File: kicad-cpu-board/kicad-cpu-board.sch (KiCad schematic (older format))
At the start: 56 parts, among them J101 ICSP Header, J102 Conn_01x10_Male, J103 Conn_01x15_Female, J104 Conn_02x05_Odd_Even, Q101 2N7000, Q102 2N7000, Q103 2N7000, Q104 2N7000, U101 L7805, U102 LP2950-3.3_TO92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

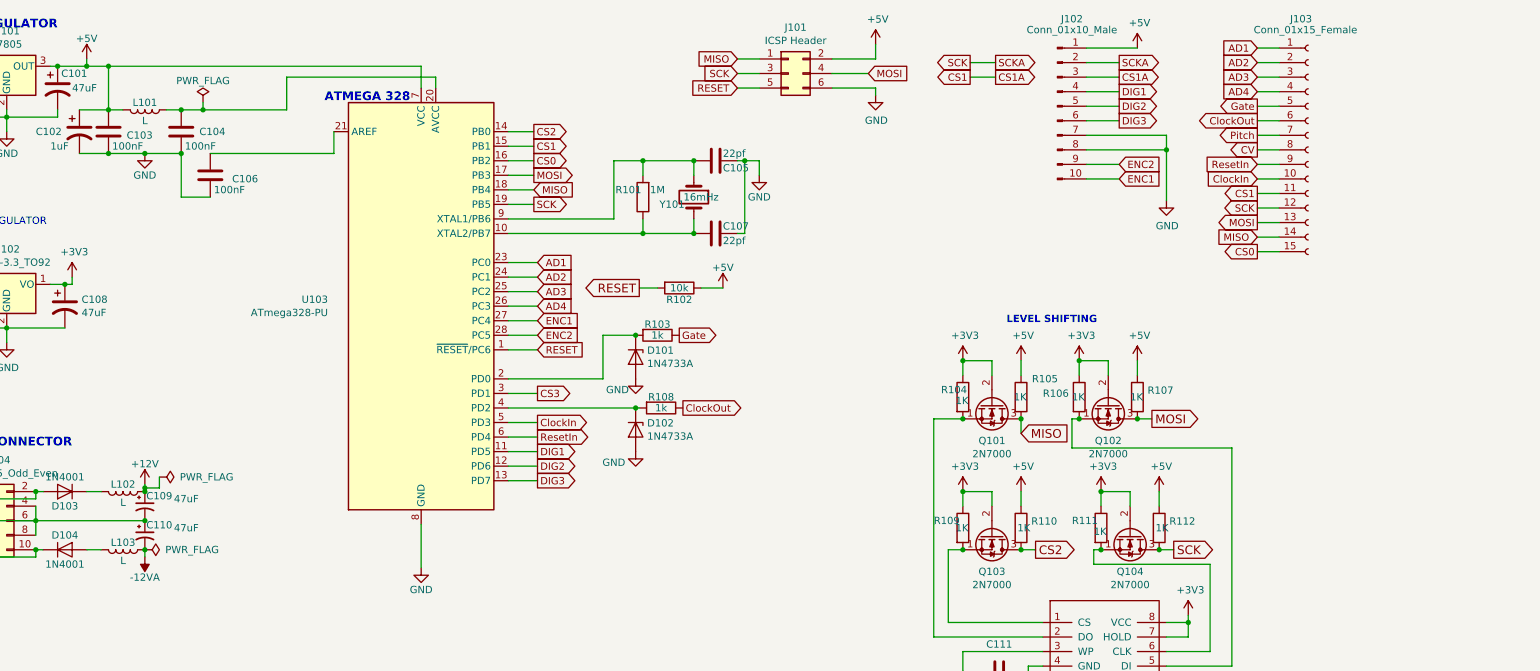
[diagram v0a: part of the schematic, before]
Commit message: Updating PCB and schematics for assembly bugfixes
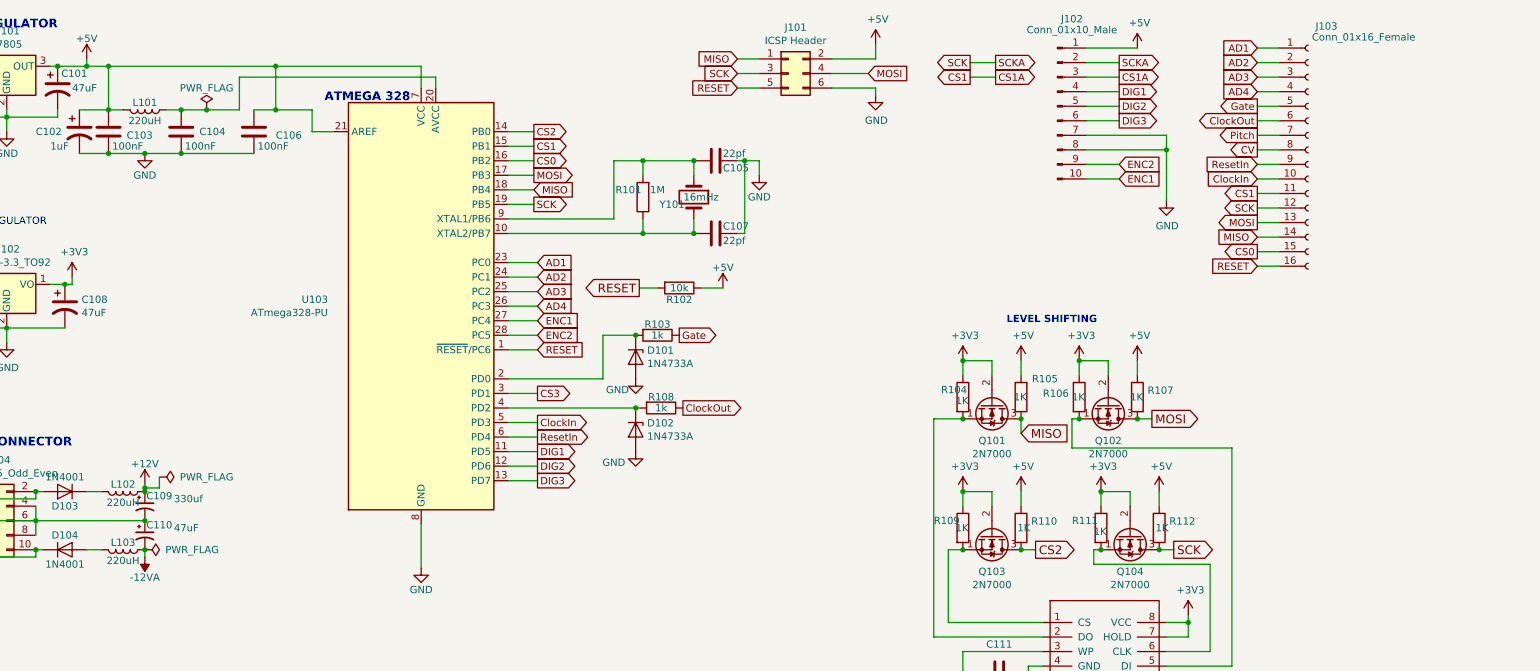
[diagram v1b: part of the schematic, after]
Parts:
- removed J103: Conn_01x15_Female, Pin_Headers:Pin_Header_Straight_1x15_Pitch2.54mm, symbol Connector:Conn_01x15_Female
- added J103: Conn_01x16_Female, Pin_Headers:Pin_Header_Straight_1x16_Pitch2.54mm, symbol Connector:Conn_01x16_Female
- C109: value 47uF -> 330uf
- L101, L102, L103: value L -> 220uH; footprint Inductors_THT:L_Axial_L5.3mm_D2.2mm_P7.62mm_Horizontal_Vishay_IM-1 -> Inductors_THT:L_Axial_L6.6mm_D2.7mm_P10.16mm_Horizontal_Vishay_IM-2
- Q101, Q102, Q103, Q104, U102: footprint TO_SOT_Packages_THT:TO-92_Inline_Narrow_Oval -> TO_SOT_Packages_THT:TO-92_Inline_Wide
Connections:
- net +5V: now also C106.1, U103.21 (AREF)
- net AD1: now also J103.1 (Pin_1)
- net AD2: now also J103.2 (Pin_2)
- net AD3: now also J103.3 (Pin_3)
- net AD4: now also J103.4 (Pin_4)
- net CS0: now also J103.15 (Pin_15)
- net CS1: now also J103.11 (Pin_11)
- net CV: now also J103.8 (Pin_8)
- net ClockIn: now also J103.10 (Pin_10)
- net ClockOut: now also J103.6 (Pin_6)
- net Gate: now also J103.5 (Pin_5)
- net MISO: now also J103.14 (Pin_14)
- net MOSI: now also J103.13 (Pin_13)
- net Pitch: now also J103.7 (Pin_7)
- net RESET: now also J103.16 (Pin_16)
- net ResetIn: now also J103.9 (Pin_9)
- net SCK: now also J103.12 (Pin_12)
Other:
- moved on the sheet: C106
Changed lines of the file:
@@
 P 2625 1400
 F 0 "L101" V 2575 1400 50  0000 C CNN
-F 1 "L" V 2700 1400 50  0000 C CNN
-F 2 "Inductors_THT:L_Axial_L5.3mm_D2.2mm_P7.62mm_Horizontal_Vishay_IM-1" H 2625 1400 50  0001 C CNN
+F 1 "220uH" V 2700 1400 50  0000 C CNN
+F 2 "Inductors_THT:L_Axial_L6.6mm_D2.7mm_P10.16mm_Horizontal_Vishay_IM-2" H 2625 1400 50  0001 C CNN
 F 3 "" H 2625 1400 50  0001 C CNN
 	1    2625 1400
@@
 L Device:C C106
 U 1 1 5CE4BC80
-P 3075 1850
-F 0 "C106" H 3225 1825 50  0000 L CNN
-F 1 "100nF" H 3100 1750 50  0000 L CNN
-F 2 "Capacitors_THT:C_Disc_D5.0mm_W2.5mm_P2.50mm" H 3113 1700 50  0001 C CNN
-F 3 "" H 3075 1850 50  0001 C CNN
-	1    3075 1850
+P 3375 1550
+F 0 "C106" H 3525 1525 50  0000 L CNN
+F 1 "100nF" H 3400 1450 50  0000 L CNN
+F 2 "Capacitors_THT:C_Disc_D5.0mm_W2.5mm_P2.50mm" H 3413 1400 50  0001 C CNN
+F 3 "" H 3375 1550 50  0001 C CNN
+	1    3375 1550
 	1    0    0    -1
 $EndComp
@@
 Wire Wire Line
 	2375 1700 2625 1700
-Wire Wire Line
-	2875 1700 2875 2000
-Wire Wire Line
-	2875 2000 3075 2000
 Connection ~ 2875 1400
 Wire Wire Line
@@
 L power:PWR_FLAG #FLG0101
 U 1 1 5B3B3D9E
-P 3025 1350
-F 0 "#FLG0101" H 3025 1425 50  0001 C CNN
-F 1 "PWR_FLAG" H 3025 1500 50  0000 C CNN
-F 2 "" H 3025 1350 50  0001 C CNN
-F 3 "" H 3025 1350 50  0001 C CNN
-	1    3025 1350
-	1    0    0    -1
-$EndComp
-Wire Wire Line
-	3025 1350 3025 1400
-Connection ~ 3025 1400
+P 3050 1400
+F 0 "#FLG0101" H 3050 1475 50  0001 C CNN
+F 1 "PWR_FLAG" H 3050 1550 50  0000 C CNN
+F 2 "" H 3050 1400 50  0001 C CNN
+F 3 "" H 3050 1400 50  0001 C CNN
+	1    3050 1400
+	1    0    0    -1
+$EndComp
 Wire Wire Line
 	2625 1700 2875 1700
-Wire Wire Line
-	2875 1400 3025 1400
 Wire Wire Line
 	2225 1100 2375 1100
@@
 F 0 "Q103" V 8700 4325 50  0000 C CNN
 F 1 "2N7000" V 8791 4325 50  0000 C CNN
-F 2 "TO_SOT_Packages_THT:TO-92_Inline_Narrow_Oval" H 8650 4250 50  0001 L CIN
+F 2 "TO_SOT_Packages_THT:TO-92_Inline_Wide" H 8650 4250 50  0001 L CIN
 F 3 "https://www.fairchildsemi.com/datasheets/2N/2N7000.pdf" H 8450 4325 50  0001 L CNN
 	1    8450 4325
@@
 F 0 "Q104" V 9650 4325 50  0000 C CNN
 F 1 "2N7000" V 9741 4325 50  0000 C CNN
-F 2 "TO_SOT_Packages_THT:TO-92_Inline_Narrow_Oval" H 9600 4250 50  0001 L CIN
+F 2 "TO_SOT_Packages_THT:TO-92_Inline_Wide" H 9600 4250 50  0001 L CIN
 F 3 "https://www.fairchildsemi.com/datasheets/2N/2N7000.pdf" H 9400 4325 50  0001 L CNN
 	1    9400 4325
@@
 F 0 "Q101" V 8700 3425 50  0000 C CNN
 F 1 "2N7000" V 8791 3425 50  0000 C CNN
-F 2 "TO_SOT_Packages_THT:TO-92_Inline_Narrow_Oval" H 8650 3350 50  0001 L CIN
+F 2 "TO_SOT_Packages_THT:TO-92_Inline_Wide" H 8650 3350 50  0001 L CIN
 F 3 "https://www.fairchildsemi.com/datasheets/2N/2N7000.pdf" H 8450 3425 50  0001 L CNN
 	1    8450 3425
@@
 F 0 "Q102" V 9500 3425 50  0000 C CNN
 F 1 "2N7000" V 9591 3425 50  0000 C CNN
-F 2 "TO_SOT_Packages_THT:TO-92_Inline_Narrow_Oval" H 9450 3350 50  0001 L CIN
+F 2 "TO_SOT_Packages_THT:TO-92_Inline_Wide" H 9450 3350 50  0001 L CIN
 F 3 "https://www.fairchildsemi.com/datasheets/2N/2N7000.pdf" H 9250 3425 50  0001 L CNN
 	1    9250 3425
@@
 F 0 "U102" H 1675 2842 50  0000 C CNN
 F 1 "LP2950-3.3_TO92" H 1675 2751 50  0000 C CNN
-F 2 "TO_SOT_Packages_THT:TO-92_Inline_Narrow_Oval" H 1675 2825 50  0001 C CIN
+F 2 "TO_SOT_Packages_THT:TO-92_Inline_Wide" H 1675 2825 50  0001 C CIN
 F 3 "http://www.ti.com/lit/ds/symlink/lp2950-n.pdf" H 1675 2550 50  0001 C CNN
 	1    1675 2600
@@
 	5125 2450 5325 2450
 $Comp
-L Connector:Conn_01x15_Female J103
-U 1 1 5DCFED35
-P 10625 1675
-F 0 "J103" H 10500 2575 50  0000 L CNN
-F 1 "Conn_01x15_Female" H 10250 2500 50  0000 L CNN
-F 2 "Pin_Headers:Pin_Header_Straight_1x15_Pitch2.54mm" H 10625 1675 50  0001 C CNN
-F 3 "~" H 10625 1675 50  0001 C CNN
-	1    10625 1675
-	1    0    0    -1
-$EndComp
-$Comp
 L Connector:Conn_01x10_Male J102
 U 1 1 5DCFEE3D
@@
 	4525 1100 4525 1250
 Wire Wire Line
-	2375 1100 4525 1100
-Wire Wire Line
-	3600 1400 3600 1175
-Wire Wire Line
-	3600 1175 4625 1175
-Wire Wire Line
 	4625 1175 4625 1250
-Wire Wire Line
-	3025 1400 3600 1400
 $Comp
 L Regulator_Linear:L7805 U101
@@
 	1    0    0    -1
 $EndComp
-Connection ~ 2875 1700
 $Comp
 L power:+12V #PWR0133
@@
 	0    1    1    0
 $EndComp
-Wire Wire Line
-	3925 1700 3925 1550
-Wire Wire Line
-	3075 1700 3925 1700
 Wire Wire Line
 	4525 4250 4525 4550
@@
 $EndComp
 $Comp
-L Device:L L103
-U 1 1 5CE903D5
-P 2475 4425
-F 0 "L103" V 2425 4425 50  0000 C CNN
-F 1 "L" V 2550 4425 50  0000 C CNN
-F 2 "Inductors_THT:L_Axial_L5.3mm_D2.2mm_P7.62mm_Horizontal_Vishay_IM-1" H 2475 4425 50  0001 C CNN
-F 3 "" H 2475 4425 50  0001 C CNN
-	1    2475 4425
-	0    1    1    0
-$EndComp
-$Comp
 L Device:L L102
 U 1 1 5CE903DB
 P 2475 4025
 F 0 "L102" V 2425 4025 50  0000 C CNN
-F 1 "L" V 2550 4025 50  0000 C CNN
-F 2 "Inductors_THT:L_Axial_L5.3mm_D2.2mm_P7.62mm_Horizontal_Vishay_IM-1" H 2475 4025 50  0001 C CNN
+F 1 "220uH" V 2550 4025 50  0000 C CNN
+F 2 "Inductors_THT:L_Axial_L6.6mm_D2.7mm_P10.16mm_Horizontal_Vishay_IM-2" H 2475 4025 50  0001 C CNN
 F 3 "" H 2475 4025 50  0001 C CNN
 	1    2475 4025
@@
 P 2625 4125
 F 0 "C109" H 2635 4195 50  0000 L CNN
-F 1 "47uF" H 2825 4175 50  0000 L CNN
+F 1 "330uf" H 2825 4175 50  0000 L CNN
 F 2 "Capacitors_THT:CP_Radial_D6.3mm_P2.50mm" H 2625 4125 50  0001 C CNN
 F 3 "" H 2625 4125 50  0001 C CNN
@@
 	1925 4425 1875 4425
 Wire Wire Line
-	2325 4425 2225 4425
-Wire Wire Line
 	2225 4025 2325 4025
 Wire Wire Line
@@
 Wire Wire Line
 	975  6150 1650 6150
+$Comp
+L Connector:Conn_01x16_Female J103
+U 1 1 5DBA0DDE
+P 10625 1675
+F 0 "J103" H 10675 2525 50  0000 L CNN
+F 1 "Conn_01x16_Female" H 10650 2450 50  0000 L CNN
+F 2 "Pin_Headers:Pin_Header_Straight_1x16_Pitch2.54mm" H 10625 1675 50  0001 C CNN
+F 3 "~" H 10625 1675 50  0001 C CNN
+	1    10625 1675
+	1    0    0    -1
+$EndComp
+Text GLabel 10275 2475 0    50   Input ~ 0
+RESET
+Wire Wire Line
+	10275 2475 10425 2475
+Wire Wire Line
+	2875 1700 3375 1700
+Connection ~ 2875 1700
+Wire Wire Line
+	3775 1550 3775 1400
+Wire Wire Line
+	3775 1550 3925 1550
+Wire Wire Line
+	3375 1400 3525 1400
+Wire Wire Line
+	3525 1400 3525 1100
+Wire Wire Line
+	2375 1100 3525 1100
+Connection ~ 3525 1400
+Wire Wire Line
+	3525 1400 3775 1400
+Connection ~ 3525 1100
+Wire Wire Line
+	3525 1100 4525 1100
+Wire Wire Line
+	2875 1400 3050 1400
+Wire Wire Line
+	3275 1400 3275 1175
+Wire Wire Line
+	3275 1175 4625 1175
+Connection ~ 3050 1400
+Wire Wire Line
+	3050 1400 3275 1400
+Wire Wire Line
+	2325 4425 2225 4425
+$Comp
+L Device:L L103
+U 1 1 5CE903D5
+P 2475 4425
+F 0 "L103" V 2425 4425 50  0000 C CNN
+F 1 "220uH" V 2550 4425 50  0000 C CNN
+F 2 "Inductors_THT:L_Axial_L6.6mm_D2.7mm_P10.16mm_Horizontal_Vishay_IM-2" H 2475 4425 50  0001 C CNN
+F 3 "" H 2475 4425 50  0001 C CNN
+	1    2475 4425
+	0    1    1    0
+$EndComp
 $EndSCHEMATC
